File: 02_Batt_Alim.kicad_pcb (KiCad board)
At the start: 2 copper layers, 58.4 x 26.7 mm, 49 parts, among them IC1 TP4056, IC2 DW01A, J1 Conn_01x01, J10 Conn_01x01, J11 Conn_01x01, J12 Conn_01x01, J2 Conn_01x01, J3 Conn_01x01, J4 Conn_01x01, J5 Conn_01x01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

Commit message: dernières modification et routage avec plan de cuivre
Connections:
- net Net-(C5-Pad1) renamed /V_BAT+_F
- net Net-(D5-Pad1) renamed /LX
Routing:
- net GND: track 164.2 -> 215.9 mm, vias 13 -> 33
- net V_chg: track 41.3 -> 40.7 mm
- added copper zone on F.Cu, net /LX
- added copper zone on F.Cu, net /V_BAT+_F
- added copper zone on F.Cu, net 5V
- added copper zone on F.Cu, net SWITCH_IN
- added copper zone on F.Cu, net SWITCH_OUT
- added copper zone on F.Cu, net V_BAT+
- added copper zone on F.Cu, net V_BAT-
- added copper zone on F.Cu, net V_OUT
- added copper zone on F.Cu, net V_chg
- added copper zone on F.Cu, net V_ext
- added copper zone on F.Cu, net V_ext_p
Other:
- board text added: "Batt_Alim 2020/12/15"
- board text removed: "Batt_Alim 2020/12/13"

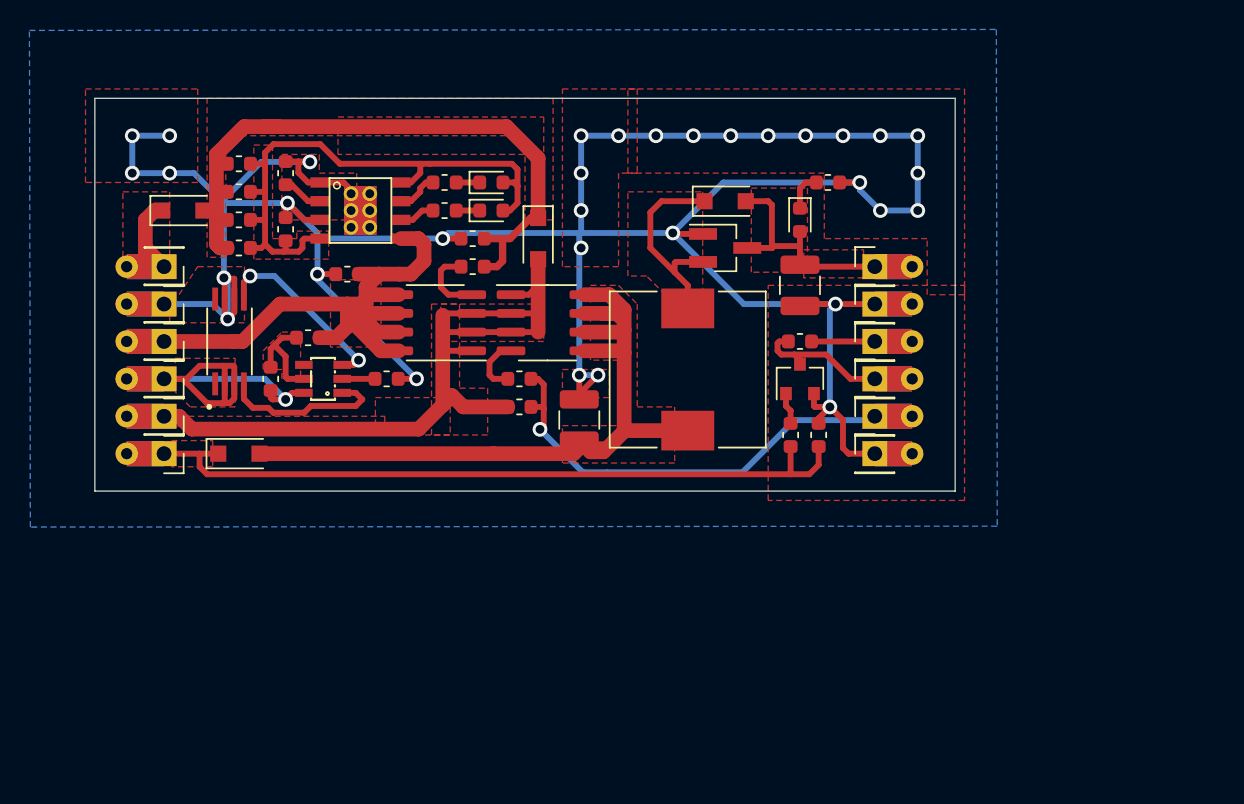
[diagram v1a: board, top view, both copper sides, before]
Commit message: corrected diodes schematics; gerbers generation
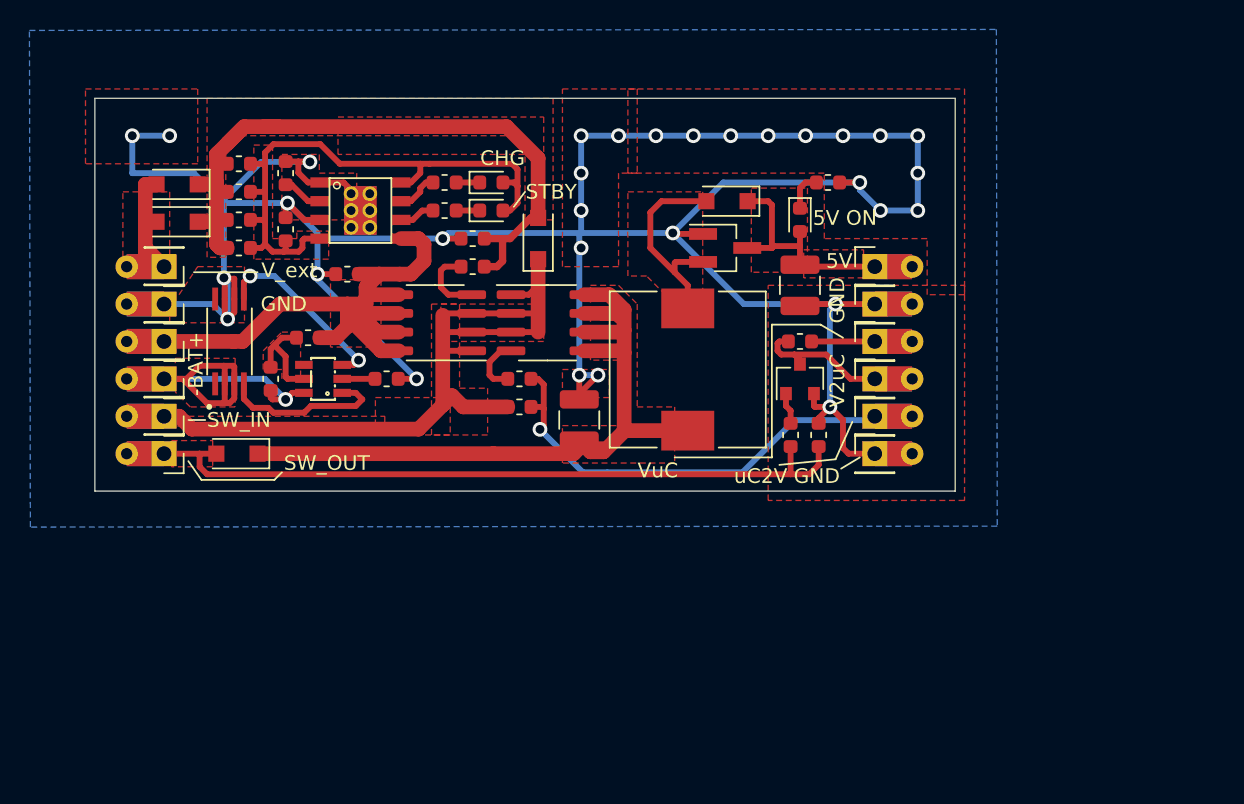
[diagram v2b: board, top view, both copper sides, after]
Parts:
- added D8: 1N5819W, Diode_SMD:D_SOD-123F, F.Cu at (105.0, 63.0)
- moved D7 1.82 mm to (105.0, 60.5), turned to 180 degrees
- moved D1 0.13 mm to (109.1, 78.7), turned to 180 degrees
- moved D5 0.13 mm to (142.4, 61.6), turned to 180 degrees
- turned D4 to 90 degrees
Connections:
- D1 pad 1: SWITCH_OUT -> V_OUT
- D1 pad 2: V_OUT -> SWITCH_OUT
- D4 pad 1: V_ext_p -> SWITCH_IN
- D4 pad 2: SWITCH_IN -> V_ext_p
- D5 pad 1: /LX -> 5V
- D5 pad 2: 5V -> /LX
- D7 pad 1: V_ext -> V_ext_p
- D7 pad 2: V_ext_p -> V_ext
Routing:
- net V_ext: track 11.5 -> 14.0 mm
- net V_ext_p: track 54.5 -> 56.5 mm
- net GND: vias 33 -> 31
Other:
- board text added: "-BAT+"
- board text added: "5V"
- board text added: "5V ON"
- board text added: "CHG"
- board text added: "GND"
- board text added: "STBY"
- board text added: "SW_IN"
- board text added: "SW_OUT"
- board text added: "V2uC"
- board text added: "V_ext"
- board text added: "VuC"
- board text added: "uC2V"

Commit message: added kicad et oshw logos
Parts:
- added REF**: OSHW-Symbol_6.7x6mm_SilkScreen, Symbol:OSHW-Symbol_6.7x6mm_SilkScreen, B.Cu at (145.8, 62.2)
- added REF**: KiCad-Logo2_5mm_SilkScreen, Symbol:KiCad-Logo2_5mm_SilkScreen, B.Cu at (121.0, 76.8)
